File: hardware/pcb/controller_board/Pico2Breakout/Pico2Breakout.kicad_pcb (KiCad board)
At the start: 2 copper layers, 145 x 100 mm, 234 parts, among them J1 430450828, J10 debug, J11 UART, J12 Conn_02x04_Odd_Even, J13 Conn_02x02_Odd_Even, J14 436500328, J15 Conn_02x02_Odd_Even, J16 436500328, J17 Conn_02x02_Odd_Even, J18 436500328, J19 Screw_Terminal_01x02, J2 430450828, J20 Screw_Terminal_01x02, J21 Screw_Terminal_01x02, J22 Conn_02x02_Odd_Even, J23 436500328, J24 Conn_02x02_Odd_Even, J25 436500328, J26 Conn_02x02_Odd_Even, J27 436500328, J28 Conn_02x02_Odd_Even, J29 x_home, J3 430450828, J30 y_home, J31 z_home, J32 a_home, J33 b_home, J34 c_input, J35 y_estop, J36 z_estop, J37 a_estop, J38 b_estop, J39 c_estop, J4 430450828, J40 E_stop, J41 x_estop, J5 430450828, J6 debug, J7 debug, J8 debug, J9 debug, K1 G3VM-61VY3, K2 G3VM-61VY3, K3 G3VM-61VY3, U1 LM5013QDDARQ1, U10 AM26LS31CD, U11 ISO7730FDWR, U12 AM26LS31CD, U13 R2SX-1205/H-R, U14 ISO7730FDWR, U15 MIC4420YM-TR, U16 MIC4420YM-TR, U17 MIC4420YM-TR, U18 TLP291-4GB-TP_ET, U19 TLP291-4GB-TP_ET, U2 LM5013QDDARQ1, U3 ISO7730FDWR, U4 AM26LS31CD, U5 ISO7730FDWR, U6 AM26LS31CD, U7 ISO7730FDWR, U8 AM26LS31CD, U9 ISO7730FDWR

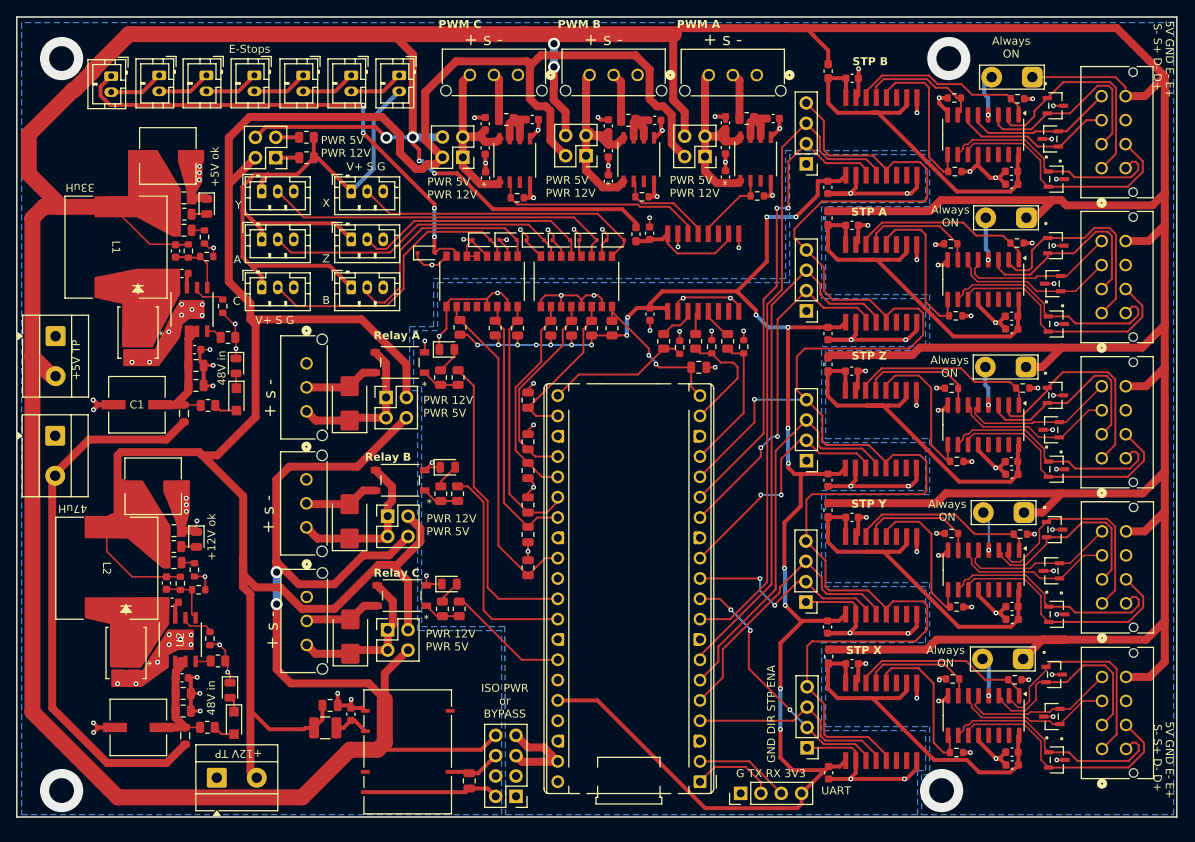
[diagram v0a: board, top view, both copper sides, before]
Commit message: Steppers (PIO) PWM (Servo+DutyCycle) and Outputs owrking
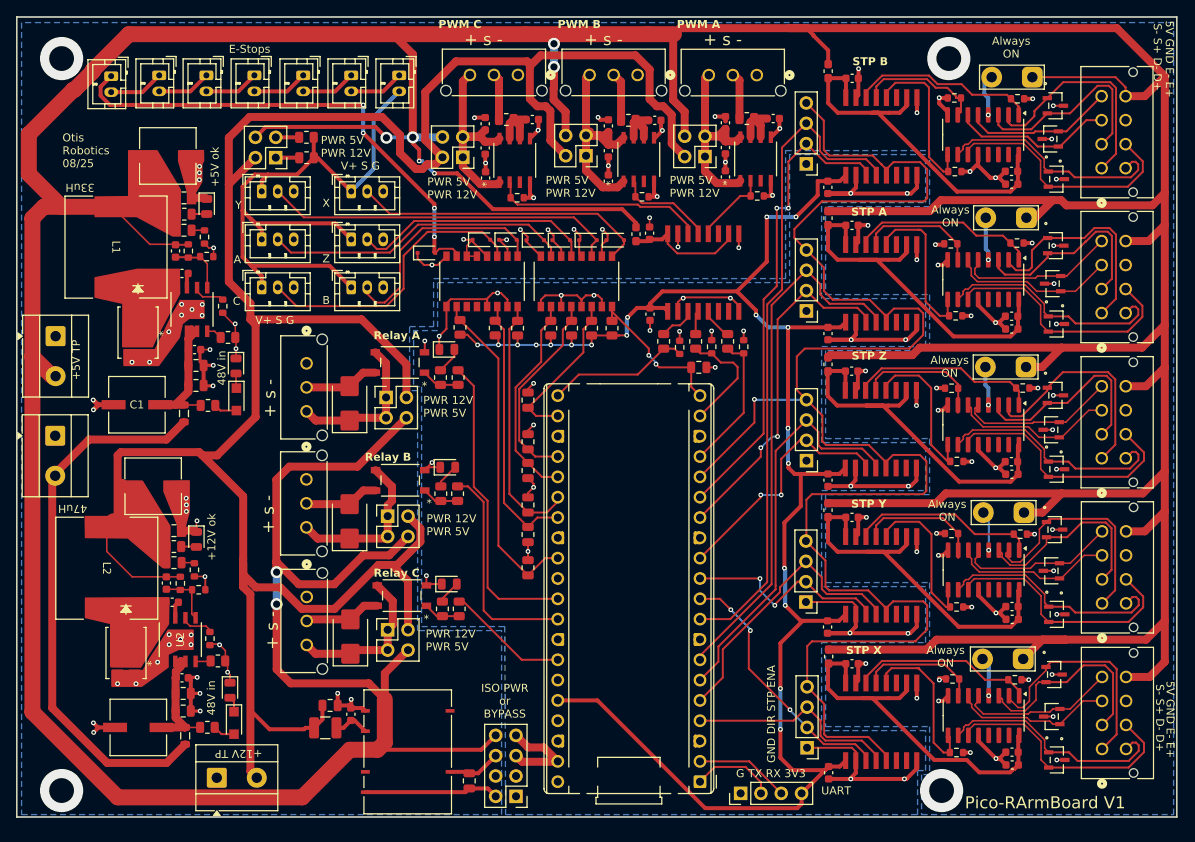
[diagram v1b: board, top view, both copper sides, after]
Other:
- board text added: "Otis Robotics 08/25"
- board text added: "Pico-RArmBoard V1"
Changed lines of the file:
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@@
 	)
 	(gr_text "V+ S G"
-		(at 85.6 59.1 0)
+		(at 84.9 59 0)
 		(layer "F.SilkS")
 		(effects
@@
 				(size 1.5 1.5)
 				(thickness 0.1875)
+			)
+			(justify left bottom)
+		)
+	)
+	(gr_text "Otis \nRobotics\n08/25"
+		(at 50.1 58.7 0)
+		(layer "F.SilkS")
+		(effects
+			(font
+				(size 1 1)
+				(thickness 0.1)
 			)
 			(justify left bottom)
@@
 		)
 	)
+	(gr_text "Pico-RArmBoard V1"
+		(at 162.9 138.9 0)
+		(layer "F.SilkS")
+		(effects
+			(font
+				(size 1.5 1.5)
+				(thickness 0.1)
+			)
+			(justify left bottom)
+		)
+	)
 	(gr_text "+ s -"
 		(at 100.3 43.5 0)
@@
 	)
 	(gr_text "S- S+ D- D+"
-		(at 186.4 128.2 270)
+		(at 186.7 123.2 270)
 		(layer "F.SilkS")
 		(effects
@@
 	)
 	(gr_text "5V GND E- E+\n"
-		(at 187.9 127.85 270)
-		(layer "F.SilkS")
-		(effects
+		(at 188 122.8 270)
+		(layer "F.SilkS")
+		(effects

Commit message: working board update
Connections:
- J11 pad 1: GNDA -> GND2
